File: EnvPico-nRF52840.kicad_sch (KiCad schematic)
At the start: 48 parts, among them J3 2.54mm header 01x20, J4 2.54mm header 01x20, J5 Conn_01x03_Male, U1 LM3671MF 3.3, U2 BQ24072RGT, U3 nRF52840, Y1 32MHz 12pF

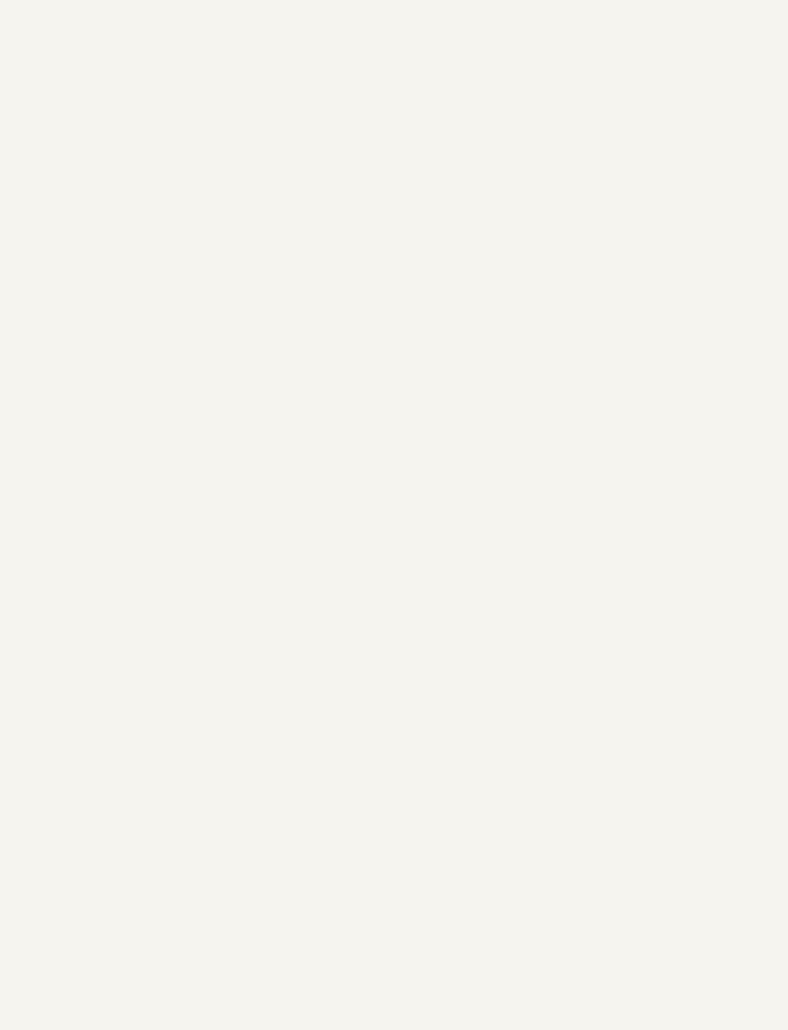
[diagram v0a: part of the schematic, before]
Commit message: preperation to potentially make a module version
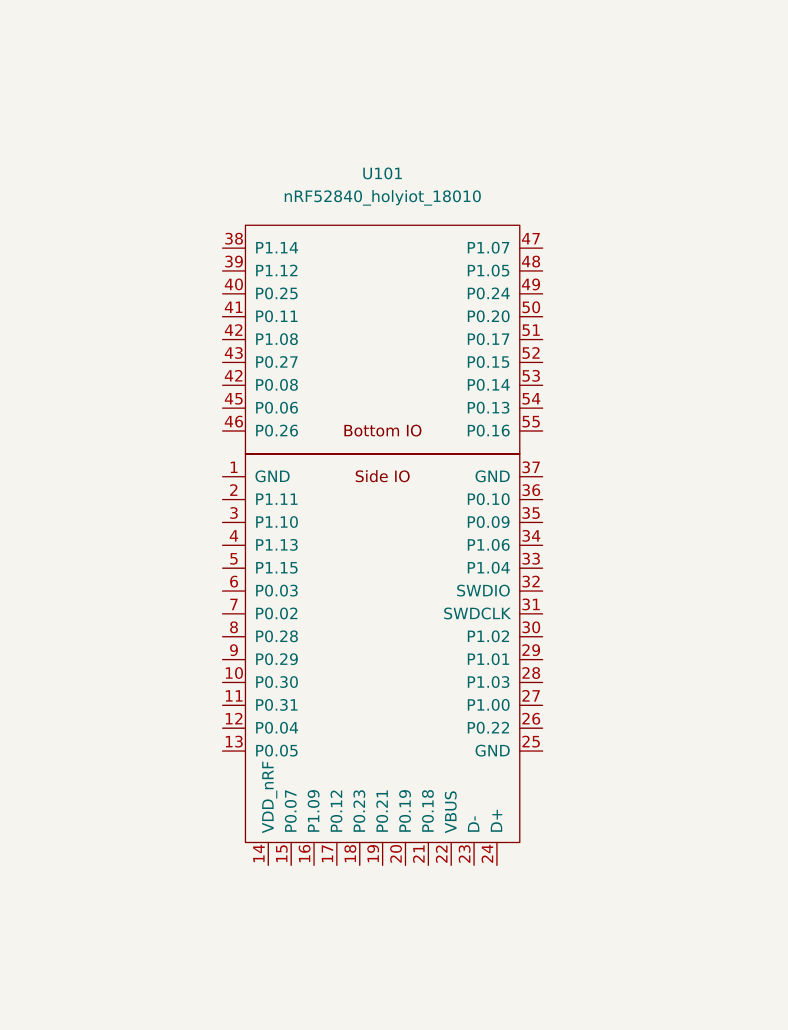
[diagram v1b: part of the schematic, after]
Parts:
- added U101: nRF52840_holyiot_18010, EnvExtras:nRF52840_holyiot_18010, symbol nrf52840_holyiot_18010:nRF52840_holyiot_18010-kicad-keyboard-parts-ahokore-resc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
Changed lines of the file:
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@@
     (pin "2")
+  )
+  (symbol (lib_id "nrf52840_holyiot_18010:nRF52840_holyiot_18010-kicad-keyboard-parts-ahokore-rescue") (at 52.07 172.085 0) (unit 1)
+    (in_bom yes) (on_board yes) (fields_autoplaced)
+    (property "Reference" "U101" (id 0) (at 52.07 132.08 0))
+    (property "Value" "nRF52840_holyiot_18010" (id 1) (at 52.07 134.62 0))
+    (property "Footprint" "EnvExtras:nRF52840_holyiot_18010" (id 2) (at 54.61 161.925 0)
+      (effects (font (size 1.27 1.27)) hide)
+    )
+    (property "Datasheet" "http://www.holyiot.com/tp/2019042516322180424.pdf" (id 3) (at 54.61 161.925 0)
+      (effects (font (size 1.27 1.27)) hide)
+    )
+    (pin "1")
+    (pin "10")
+    (pin "11")
+    (pin "12")
+    (pin "13")
+    (pin "14")
+    (pin "15")
+    (pin "16")
+    (pin "17")
+    (pin "18")
+    (pin "19")
+    (pin "2")
+    (pin "20")
+    (pin "21")
+    (pin "22")
+    (pin "23")
+    (pin "24")
+    (pin "25")
+    (pin "26")
+    (pin "27")
+    (pin "28")
+    (pin "29")
+    (pin "3")
+    (pin "30")
+    (pin "31")
+    (pin "32")
+    (pin "33")
+    (pin "34")
+    (pin "35")
+    (pin "36")
+    (pin "37")
+    (pin "38")
+    (pin "39")
+    (pin "4")
+    (pin "40")
+    (pin "41")
+    (pin "42")
+    (pin "42")
+    (pin "43")
+    (pin "45")
+    (pin "46")
+    (pin "47")
+    (pin "48")
+    (pin "49")
+    (pin "5")
+    (pin "50")
+    (pin "51")
+    (pin "52")
+    (pin "53")
+    (pin "54")
+    (pin "55")
+    (pin "6")
+    (pin "7")
+    (pin "8")
+    (pin "9")
   )
   (symbol (lib_id "Device:C_Small") (at 215.9 82.55 270) (unit 1)
@@
       (reference "U3") (unit 1) (value "nRF52840") (footprint "Package_DFN_QFN:Nordic_AQFN-73-1EP_7x7mm_P0.5mm")
     )
+    (path "/8ee0b195-44f0-4b21-9341-8dba1a90f90e"
+      (reference "U101") (unit 1) (value "nRF52840_holyiot_18010") (footprint "EnvExtras:nRF52840_holyiot_18010")
+    )
     (path "/00000000-0000-0000-0000-00005edb7d8d"
